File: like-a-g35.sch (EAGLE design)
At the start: 17 parts, among them J1 AVR_SPI_PRG_62X3_LOCK, Q1 16MHz, X1 S1, X2 S2, X3 S3, X4 POWER

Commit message: 0.9.
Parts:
- removed C1, C2: 18pF, programmer:CAP0805
- removed C3, C5: 0.1uF, programmer:CAP0805
- removed C4: 10uF, programmer:CAP_POL1206
- removed J1: AVR_SPI_PRG_62X3_LOCK, programmer:AVR_SPI_PRG_62X3_LOCK
- removed Q1: 16MHz, crystal:CRYSTALHC49S
- removed R1, R2: 22, like-a-g35:RESISTOR0805-RES
- removed R3: 10K, like-a-g35:RESISTOR0805-RES
- removed U$3: BUTTON_TD-85XU, programmer:BUTTON_TD-85XU
- added U1: ARDUINOR3-DIMENSION, adafruit:ARDUINOR3-DIMENSION
- added X5, X6: POWER, con-ptr500:AK300/2
- added X7: WS1, con-ptr500:AK300/2
- added X8: WS2, con-ptr500:AK300/2
- added X9: WS3, con-ptr500:AK300/2
- U$1: value ATMEGA32U4-AU -> PNA460XM; device like-a-g35:ATMEGA32U4-AU -> adafruit:PNA460XM
- X1: value S1 -> G1
- X2: value S2 -> G2
- X3: value S3 -> G3
- renumbered U$2 to U2
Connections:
- removed net !RESET: J1.5, U$1./RESET
- removed net 3V3: C5.1, U$1.UCAP
- removed net D+: R2.2, U$1.D+
- removed net D-: R1.2, U$1.D-
- removed net MISO: J1.1, U$1.PB3(PDO/MISO)
- removed net MOSI: J1.4, U$1.PB2(PDI/MOSI)
- removed net N$1: R3.1, U$1.PE2(!HWB), U$3.P$1
- removed net RAW_D+: R2.1, U2.D+
- removed net RAW_D-: R1.1, U2.D-
- removed net SCK: J1.3, U$1.PB1(SCK)
- removed net XTAL1: C1.1, Q1.2, U$1.XTAL1
- removed net XTAL2: C2.1, Q1.1, U$1.XTAL2
- new net CLK1: U1.D3, X7-2.KL
- new net CLK2: U1.D5, X8-2.KL
- new net CLK3: U1.D7, X9-2.KL
- new net DATA1: U1.D2, X7-1.KL
- new net DATA2: U1.D4, X8-1.KL
- new net DATA3: U1.D6, X9-1.KL
- new net GDATA1: U1.D8, X1-2.KL
- new net GDATA2: U1.D9, X2-2.KL
- new net GDATA3: U1.D10, X3-2.KL
- new net IR-OUT: U$1.OUT, U1.D11
- net +5V: now also U1.5V, X5-1.KL, X6-1.KL; no longer C3.1, C4.+, J1.2, R3.2, U$1.AVCC, U$1.AVCC1, U$1.UVCC, U$1.VBUS, U$1.VCC1
- net GND: now also U1.GND, U1.GND1, U1.GND2, X5-2.KL, X6-2.KL; no longer C1.2, C2.2, C3.2, C4.-, C5.2, J1.6, U$1.GND1, U$1.GND2, U$1.GND3, U$1.UGND, U$3.P$2
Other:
- moved on the sheet: X1-1, X1-2, X1-3, X2-1, X2-2, X2-3, X3-1, X3-2, X3-3

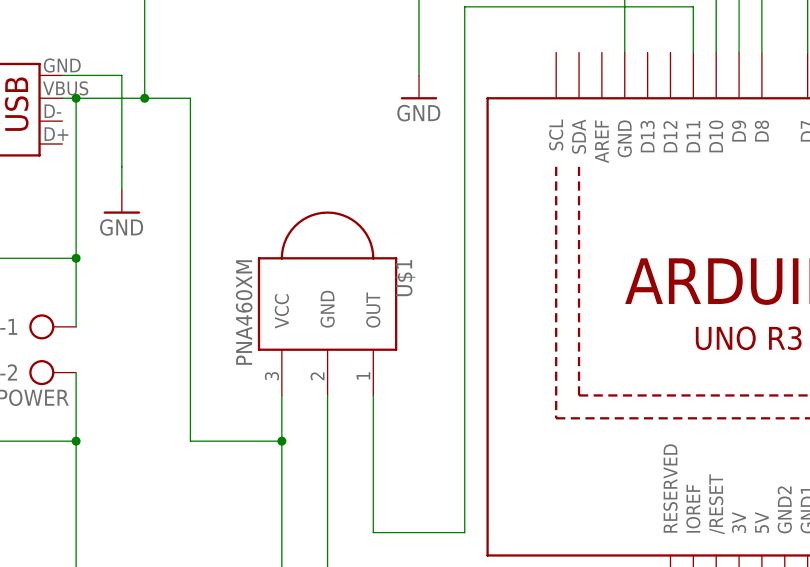
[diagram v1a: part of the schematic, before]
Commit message: Minor adjustments after previewing at OSH Park.
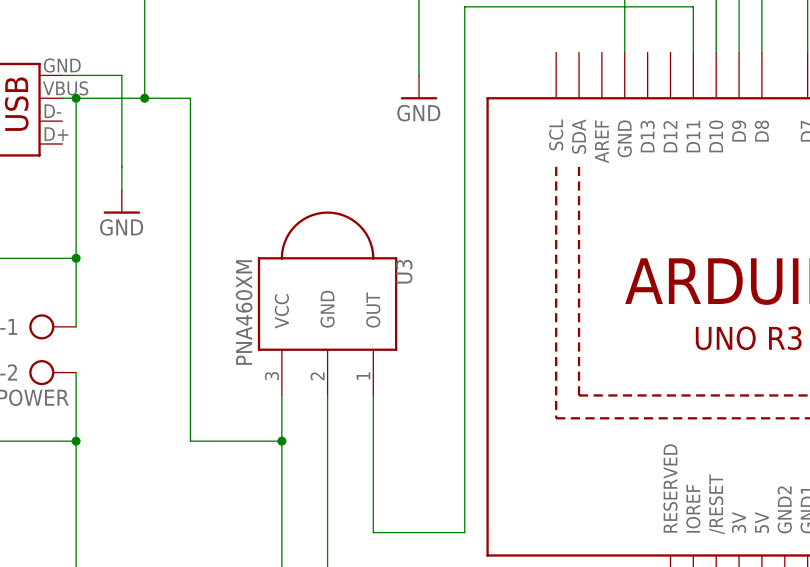
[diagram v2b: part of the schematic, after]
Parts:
- renumbered U$1 to U3
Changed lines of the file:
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@@
 <attribute name="OC_NEWARK" value="unknown"/>
 </part>
-<part name="U$1" library="adafruit" deviceset="PNA460XM" device=""/>
+<part name="U3" library="adafruit" deviceset="PNA460XM" device=""/>
 </parts>
 <sheets>
@@
 <instance part="X9" gate="-1" x="129.54" y="96.52"/>
 <instance part="X9" gate="-2" x="129.54" y="91.44"/>
-<instance part="U$1" gate="G$1" x="30.48" y="55.88" rot="R270"/>
+<instance part="U3" gate="G$1" x="30.48" y="55.88" rot="R270"/>
 </instances>
 <busses>
@@
 <wire x1="-30.48" y1="60.96" x2="-30.48" y2="53.34" width="0.1524" layer="91"/>
 <junction x="-12.7" y="60.96"/>
-<pinref part="U$1" gate="G$1" pin="VCC"/>
+<pinref part="U3" gate="G$1" pin="VCC"/>
 <wire x1="25.4" y1="45.72" x2="25.4" y2="40.64" width="0.1524" layer="91"/>
 <wire x1="25.4" y1="40.64" x2="15.24" y2="40.64" width="0.1524" layer="91"/>
@@
 <wire x1="-30.48" y1="40.64" x2="-30.48" y2="48.26" width="0.1524" layer="91"/>
 <junction x="-12.7" y="40.64"/>
-<pinref part="U$1" gate="G$1" pin="GND"/>
+<pinref part="U3" gate="G$1" pin="GND"/>
 <wire x1="30.48" y1="45.72" x2="30.48" y2="17.78" width="0.1524" layer="91"/>
 <junction x="30.48" y="17.78"/>
@@
 <net name="IR-OUT" class="0">
 <segment>
-<pinref part="U$1" gate="G$1" pin="OUT"/>
+<pinref part="U3" gate="G$1" pin="OUT"/>
 <wire x1="35.56" y1="45.72" x2="35.56" y2="30.48" width="0.1524" layer="91"/>
 <wire x1="35.56" y1="30.48" x2="45.72" y2="30.48" width="0.1524" layer="91"/>
